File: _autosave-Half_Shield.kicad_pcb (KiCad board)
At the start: 2 copper layers, 74.9 x 114.2 mm, 44 parts, among them U1 TPS561208DDC

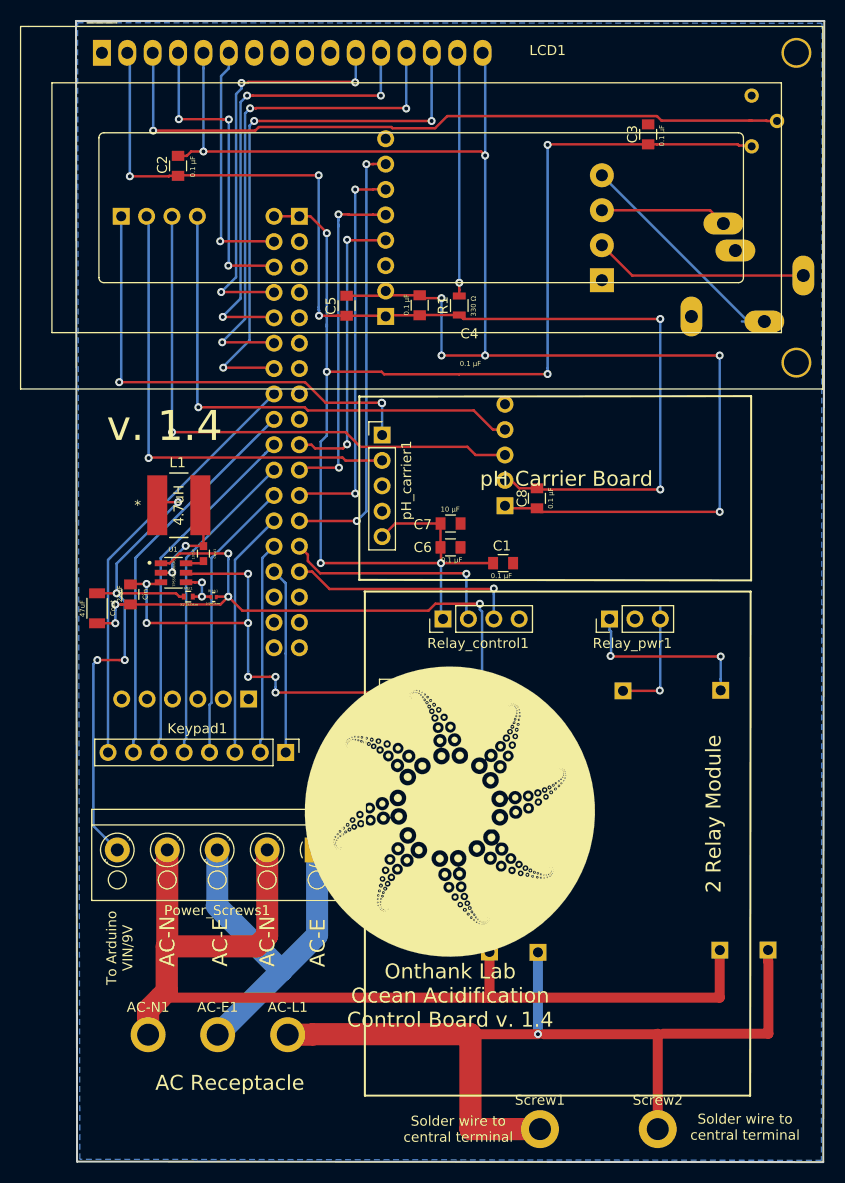
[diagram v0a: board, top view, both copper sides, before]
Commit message: first attempt at buck converter
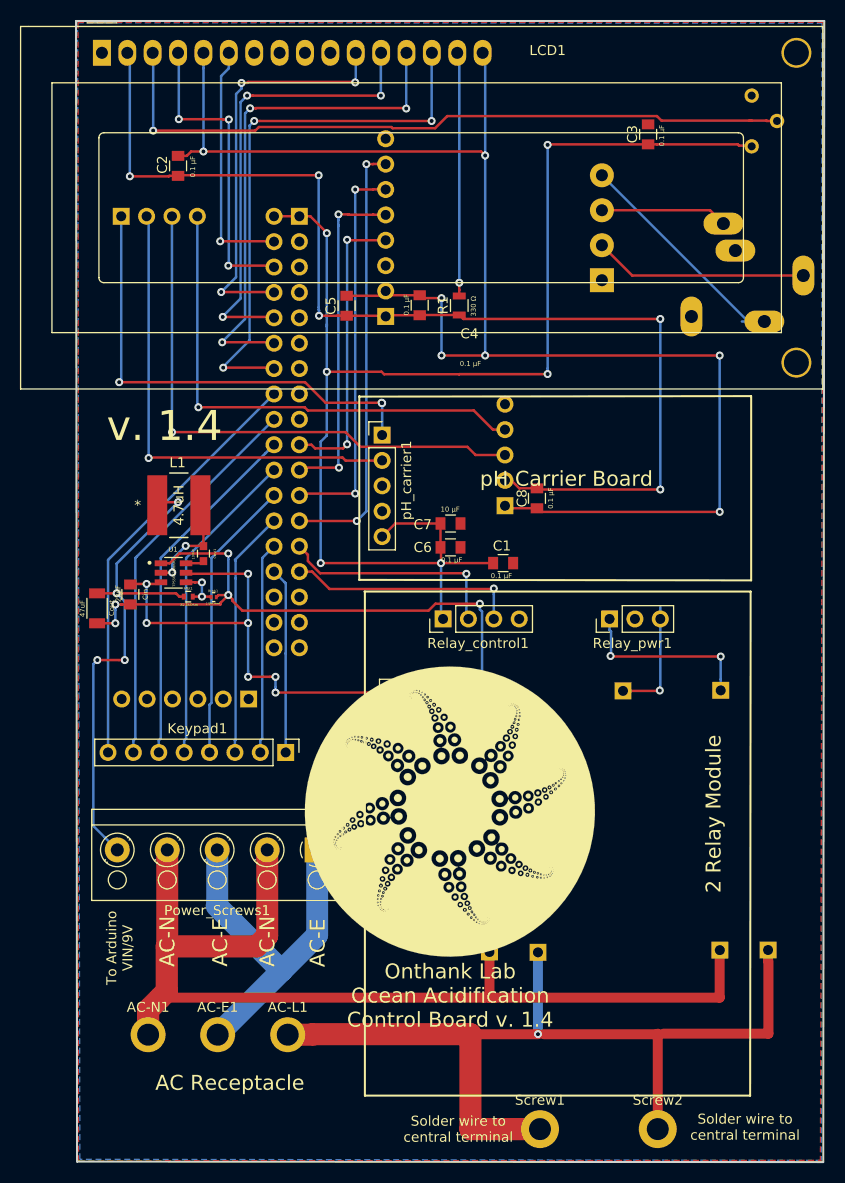
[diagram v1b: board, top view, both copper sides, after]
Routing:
- added copper zone on F.Cu, net GND
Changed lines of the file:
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@@
     (thickness 1.6)
     (drawings 78)
-    (tracks 524)
+    (tracks 531)
     (zones 0)
     (modules 44)
@@
   (page A4)
   (layers
-    (0 F.Cu signal hide)
-    (31 B.Cu signal hide)
-    (32 B.Adhes user)
-    (33 F.Adhes user)
-    (34 B.Paste user)
-    (35 F.Paste user)
-    (36 B.SilkS user)
-    (37 F.SilkS user)
-    (38 B.Mask user)
-    (39 F.Mask user)
-    (40 Dwgs.User user)
-    (41 Cmts.User user)
-    (42 Eco1.User user)
-    (43 Eco2.User user)
-    (44 Edge.Cuts user)
-    (45 Margin user)
-    (46 B.CrtYd user)
-    (47 F.CrtYd user)
+    (0 F.Cu signal)
+    (31 B.Cu signal)
+    (32 B.Adhes user hide)
+    (33 F.Adhes user hide)
+    (34 B.Paste user hide)
+    (35 F.Paste user hide)
+    (36 B.SilkS user hide)
+    (37 F.SilkS user hide)
+    (38 B.Mask user hide)
+    (39 F.Mask user hide)
+    (40 Dwgs.User user hide)
+    (41 Cmts.User user hide)
+    (42 Eco1.User user hide)
+    (43 Eco2.User user hide)
+    (44 Edge.Cuts user hide)
+    (45 Margin user hide)
+    (46 B.CrtYd user hide)
+    (47 F.CrtYd user hide)
     (48 B.Fab user hide)
-    (49 F.Fab user)
+    (49 F.Fab user hide)
   )
   (setup
@@
       (effects (font (size 0.5 0.5) (thickness 0.125)))
     )
-    (fp_text value 22uF (at -0.0668 1.0668 90) (layer F.SilkS)
+    (fp_text value 22uF (at -0.0856 1.2192 90) (layer F.SilkS)
       (effects (font (size 0.5 0.5) (thickness 0.125)))
     )
@@
     (fp_line (start 1 0.62) (end -1 0.62) (layer F.Fab) (width 0.1))
     (fp_line (start -1 0.62) (end -1 -0.62) (layer F.Fab) (width 0.1))
-    (fp_text user %R (at -0.016 -1.27 90) (layer F.Fab)
+    (fp_text user %R (at -0.016 -1.27 90) (layer F.Fab) hide
       (effects (font (size 0.5 0.5) (thickness 0.0625)))
     )
@@
     (tags "capacitor 1206")
     (attr smd)
-    (fp_text reference Cout (at -0.0268 -1.5748 270) (layer F.SilkS)
+    (fp_text reference Cout (at -0.0268 -1.4478 270) (layer F.SilkS)
       (effects (font (size 0.5 0.5) (thickness 0.125)))
     )
@@
     (fp_line (start 1.6 0.8) (end -1.6 0.8) (layer F.Fab) (width 0.1))
     (fp_line (start -1.6 0.8) (end -1.6 -0.8) (layer F.Fab) (width 0.1))
-    (fp_text user %R (at -0.0776 -1.524 90) (layer F.Fab)
+    (fp_text user %R (at -0.0776 -1.524 90) (layer F.Fab) hide
       (effects (font (size 0.5 0.5) (thickness 0.125)))
     )
@@
   (segment (start 125.520199 104.21452) (end 125.520199 86.150701) (width 0.25) (layer B.Cu) (net 5))
   (segment (start 125.520199 86.150701) (end 126.6952 84.9757) (width 0.25) (layer B.Cu) (net 5) (status 20))
-  (segment (start 122.7836 105.6132) (end 122.7836 104.411119) (width 0.25) (layer B.Cu) (net 6) (status 10))
   (segment (start 122.7836 104.411119) (end 122.790201 104.404518) (width 0.25) (layer B.Cu) (net 6))
-  (segment (start 122.790201 104.404518) (end 122.790201 86.340699) (width 0.25) (layer B.Cu) (net 6))
   (segment (start 122.790201 86.340699) (end 126.6952 82.4357) (width 0.25) (layer B.Cu) (net 6) (status 20))
   (segment (start 134.9756 82.4484) (end 129.2479 82.4484) (width 0.25) (layer F.Cu) (net 7) (status 20))
@@
   (segment (start 137.398 59.9092) (end 137.8712 59.436) (width 0.25) (layer F.Cu) (net 1))
   (segment (start 133.9596 59.9092) (end 137.398 59.9092) (width 0.25) (layer F.Cu) (net 1))
+  (segment (start 122.848201 86.398699) (end 122.848201 88.202601) (width 0.25) (layer B.Cu) (net 6))
+  (segment (start 122.790201 86.340699) (end 122.848201 86.398699) (width 0.25) (layer B.Cu) (net 6))
+  (segment (start 122.7836 104.411119) (end 122.7836 105.6132) (width 0.25) (layer B.Cu) (net 6))
+  (segment (start 122.848201 104.346518) (end 122.7836 104.411119) (width 0.25) (layer B.Cu) (net 6))
+  (segment (start 122.848201 88.202601) (end 122.848201 104.346518) (width 0.25) (layer B.Cu) (net 6))
   (segment (start 138.5824 99.6188) (end 126.8476 99.6188) (width 0.25) (layer F.Cu) (net 33))
   (segment (start 126.8476 99.6188) (end 126.8476 99.6188) (width 0.25) (layer F.Cu) (net 33))
@@
   (via (at 122.1232 85.6996) (size 0.8) (drill 0.4) (layers F.Cu B.Cu) (net 36))
   (segment (start 122.1232 85.6996) (end 122.1232 86.265285) (width 0.25) (layer B.Cu) (net 36))
-  (segment (start 122.1232 86.265285) (end 122.1232 90.0176) (width 0.25) (layer B.Cu) (net 36))
-  (segment (start 122.1232 90.0176) (end 122.1232 90.0176) (width 0.25) (layer B.Cu) (net 36))
-  (via (at 122.1232 90.0176) (size 0.8) (drill 0.4) (layers F.Cu B.Cu) (net 36))
   (segment (start 120.9668 90.0176) (end 120.916 90.0684) (width 0.25) (layer F.Cu) (net 36))
-  (segment (start 122.1232 90.0176) (end 120.9668 90.0176) (width 0.25) (layer F.Cu) (net 36))
-  (segment (start 121.3424 90.7984) (end 122.1232 90.0176) (width 0.25) (layer F.Cu) (net 36))
-  (segment (start 112.3188 90.7984) (end 121.3424 90.7984) (width 0.25) (layer F.Cu) (net 36))
   (segment (start 111.4438 90.7984) (end 111.4372 90.805) (width 0.25) (layer F.Cu) (net 36))
   (segment (start 112.3188 90.7984) (end 111.4438 90.7984) (width 0.25) (layer F.Cu) (net 36))
@@
   (segment (start 110.8202 92.6846) (end 108.9942 92.6846) (width 0.25) (layer F.Cu) (net 36))
   (segment (start 142.158699 91.420699) (end 142.850598 90.7288) (width 0.25) (layer F.Cu) (net 36))
-  (segment (start 122.1232 90.0176) (end 123.526299 91.420699) (width 0.25) (layer F.Cu) (net 36))
-  (segment (start 123.526299 91.420699) (end 142.158699 91.420699) (width 0.25) (layer F.Cu) (net 36))
   (segment (start 142.850598 90.7288) (end 147.2946 90.7288) (width 0.25) (layer F.Cu) (net 36))
   (segment (start 147.2946 90.7288) (end 147.2946 90.7288) (width 0.25) (layer F.Cu) (net 36))
@@
   (segment (start 147.2946 91.294485) (end 147.516599 91.516484) (width 0.25) (layer B.Cu) (net 36))
   (segment (start 147.2946 90.7288) (end 147.2946 91.294485) (width 0.25) (layer B.Cu) (net 36))
+  (segment (start 122.1232 86.265285) (end 122.1232 89.8652) (width 0.25) (layer B.Cu) (net 36))
+  (segment (start 122.1232 89.8652) (end 122.1232 89.8652) (width 0.25) (layer B.Cu) (net 36))
+  (via (at 122.1232 89.8652) (size 0.8) (drill 0.4) (layers F.Cu B.Cu) (net 36))
+  (segment (start 121.1192 89.8652) (end 120.916 90.0684) (width 0.25) (layer F.Cu) (net 36))
+  (segment (start 122.1232 89.8652) (end 121.1192 89.8652) (width 0.25) (layer F.Cu) (net 36))
+  (segment (start 123.526299 91.420699) (end 142.158699 91.420699) (width 0.25) (layer F.Cu) (net 36))
+  (segment (start 122.523199 90.417599) (end 123.526299 91.420699) (width 0.25) (layer F.Cu) (net 36))
+  (segment (start 122.523199 90.265199) (end 122.523199 90.417599) (width 0.25) (layer F.Cu) (net 36))
+  (segment (start 122.1232 89.8652) (end 122.523199 90.265199) (width 0.25) (layer F.Cu) (net 36))
+  (segment (start 121.3424 90.7984) (end 121.3424 90.646) (width 0.25) (layer F.Cu) (net 36))
+  (segment (start 112.3188 90.7984) (end 121.3424 90.7984) (width 0.25) (layer F.Cu) (net 36))
+  (segment (start 121.3424 90.646) (end 122.1232 89.8652) (width 0.25) (layer F.Cu) (net 36))
   (segment (start 119.634 81.1784) (end 119.3292 80.8736) (width 0.25) (layer F.Cu) (net 37))
   (segment (start 119.634 84.9616) (end 119.634 81.1784) (width 0.25) (layer F.Cu) (net 37))
@@
       )
     )
+  )
+  (zone (net 1) (net_name GND) (layer F.Cu) (hatch edge 0.508)
+    (connect_pads (clearance 0.508))
+    (min_thickness 0.254)
+    (fill yes (arc_segments 16) (thermal_gap 0.508) (thermal_bridge_width 0.508))
+    (polygon
+      (pts
+        (xy 181.3814 146.5834) (xy 181.6608 32.5628) (xy 107.0864 32.5628) (xy 107.1372 146.4818) (xy 181.4576 146.431)
+        (xy 181.356 146.4564)
+      )
+    )
